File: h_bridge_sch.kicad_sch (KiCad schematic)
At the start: 17 parts, among them Q1 BC817, Q2 BC817, Q3 BC807, Q4 NMOS, Q5 NMOS, Q6 BC817, Q7 BC817, Q8 BC807

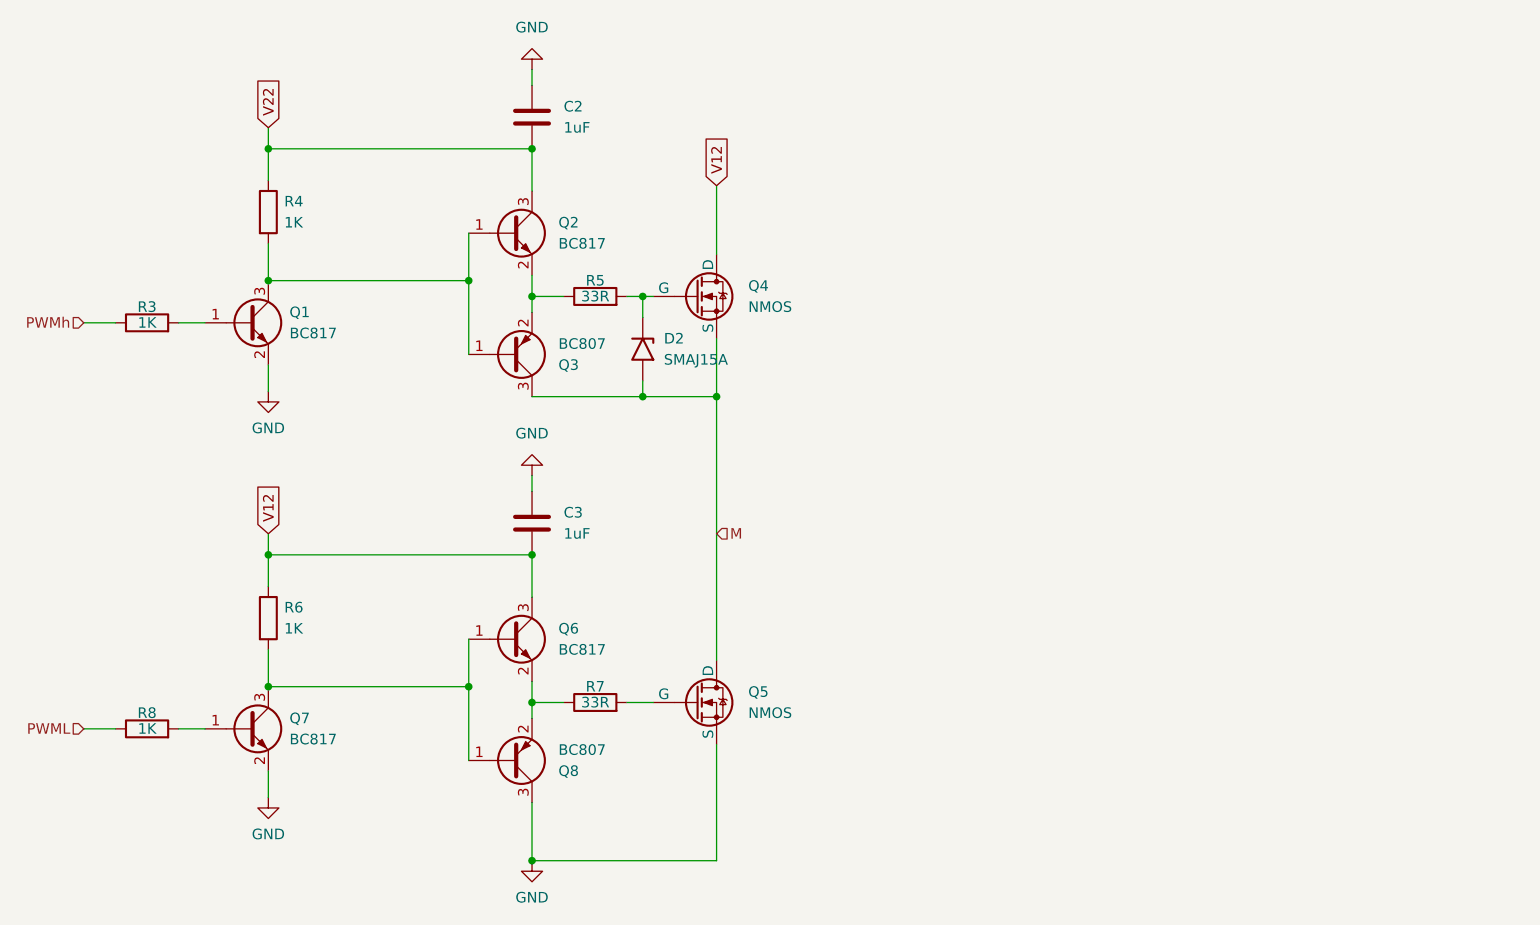
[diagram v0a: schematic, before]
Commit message: alteração no circuito de ponte h e inicio da criação da PCB
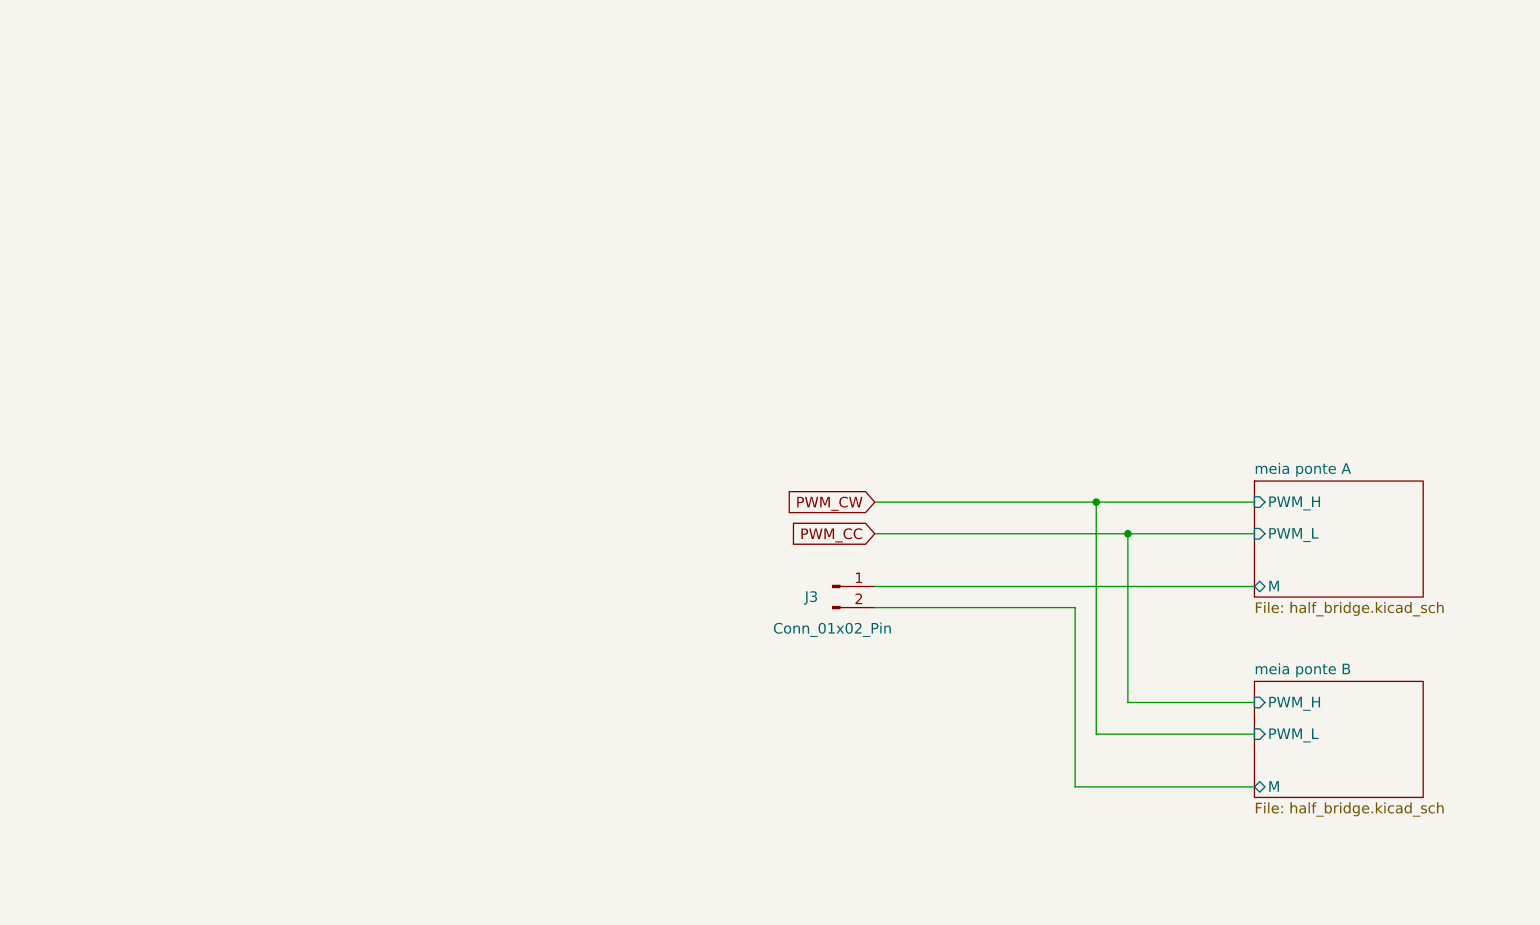
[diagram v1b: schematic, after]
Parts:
- removed C2, C3: 1uF, symbol Device:C
- removed D2: SMAJ15A, Diode_SMD:D_SMA, symbol Diode:SMAJ15A
- removed Q1, Q2, Q6, Q7: BC817, Package_TO_SOT_SMD:SOT-23, symbol Transistor_BJT:BC817
- removed Q3, Q8: BC807, Package_TO_SOT_SMD:SOT-23, symbol Transistor_BJT:BC807
- removed Q4, Q5: NMOS, Package_TO_SOT_SMD:TO-252-3_TabPin2, symbol Simulation_SPICE:NMOS
- removed R3, R4, R6, R8: 1K, symbol Device:R
- removed R5, R7: 33R, symbol Device:R
- added J3: Conn_01x02_Pin, TerminalBlock_TE-Connectivity:TerminalBlock_TE_282843-2_1x02_P10.16mm_Horizontal, symbol Connector:Conn_01x02_Pin
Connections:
- new net meia ponte A/M: J3.1 (Pin_1)
- new net meia ponte B/M: J3.2 (Pin_2)
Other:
- added sheet meia ponte A (half_bridge.kicad_sch)
- added sheet meia ponte B (half_bridge.kicad_sch)
